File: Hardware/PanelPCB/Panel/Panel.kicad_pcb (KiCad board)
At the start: 2 copper layers, 22 x 32 mm, 13 parts, among them J1 RJ45, J2 Conn_01x03_Socket, U1 AP2204R-5.0, U2 SN74LV1T34DBV

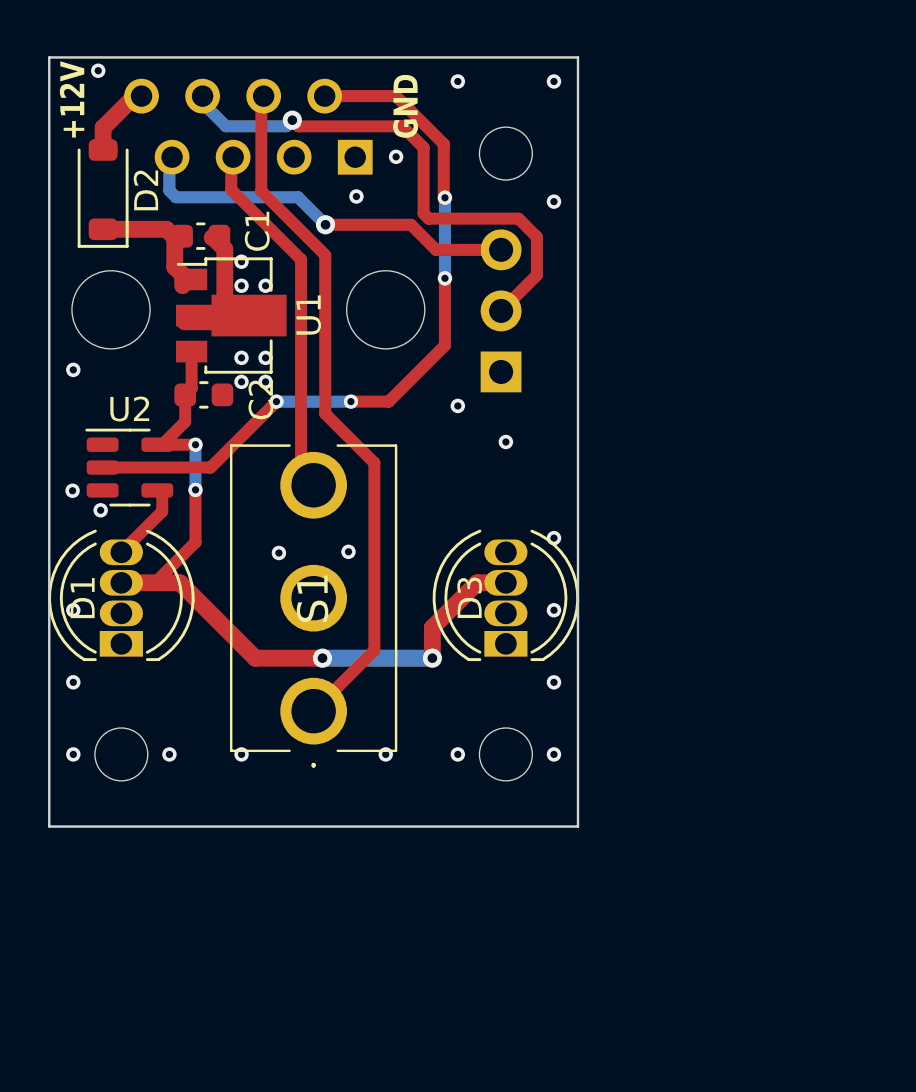
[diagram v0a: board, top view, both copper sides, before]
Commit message: update ControlPanel PCB
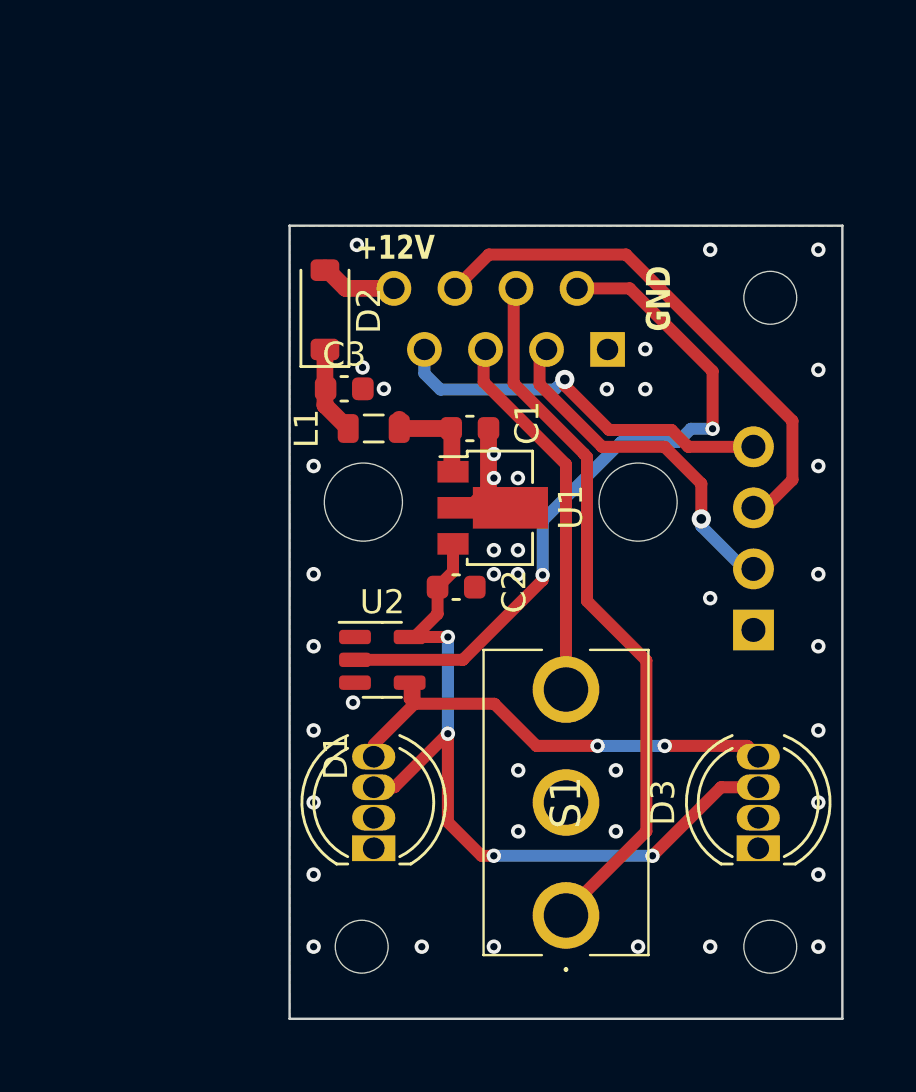
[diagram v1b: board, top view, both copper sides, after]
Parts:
- added C3: 100nF, Capacitor_SMD:C_0603_1608Metric, F.Cu at (152.3, 73.8)
- added L1: L_Ferrite, Inductor_SMD:L_0805_2012Metric, F.Cu at (153.5, 75.4)
- J2: footprint Connector_PinHeader_2.54mm:PinHeader_1x03_P2.54mm_Vertical -> Connector_PinHeader_2.54mm:PinHeader_1x04_P2.54mm_Vertical
- moved J2 15.0 mm to (169.3, 83.8)
- moved C1 13.8 mm to (157.5, 75.4)
- moved H3 13.6 mm to (170.0, 97.0)
- moved U1 13.5 mm to (158.8, 78.7)
- moved C2 13.2 mm to (156.9, 82.0)
- moved J1 13.2 mm to (163.2, 72.2)
- moved U2 13.2 mm to (153.9, 85.1)
- moved H2 12.8 mm to (153.0, 97.0)
- moved H1 12.5 mm to (170.0, 70.0)
- moved D1 12.4 mm to (153.5, 91.0)
- moved D3 12.4 mm to (169.5, 91.0)
- moved S1 11.2 mm to (161.5, 91.0)
- moved D2 10.5 mm to (151.5, 70.5)
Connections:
- C1 pad 1: Net-(D2-K) -> Net-(U1-VIN)
- J1 pad 3: unconnected-(J1-Pad3) -> OUT2
- J2 pad 2: IN3 -> OUT2
- J2 pad 3: IN4 -> IN3
- U1 pad 1: Net-(D2-K) -> Net-(U1-VIN)
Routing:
- net OUT_1: track 3.28 -> 19.5 mm, vias 0 -> 2
- net OUT2: track 0.00 -> 14.7 mm, vias 0 -> 1
- net Net-(U1-VIN): track 0.00 -> 4.37 mm
- net Net-(D2-K): track 5.00 -> 3.69 mm
- net IN1: track 28.7 -> 29.5 mm
- net OUT1: track 30.6 -> 29.8 mm, vias 4 -> 2
- net GND1: track 5.13 -> 4.28 mm, vias 31 -> 41
- net +5V: track 33.2 -> 32.5 mm
- net IN3: track 22.1 -> 22.0 mm, vias 1 -> 0
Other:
- board size 22 x 32 mm -> 23 x 33 mm

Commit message: update PanelPCB and generade a DualPanelPCB
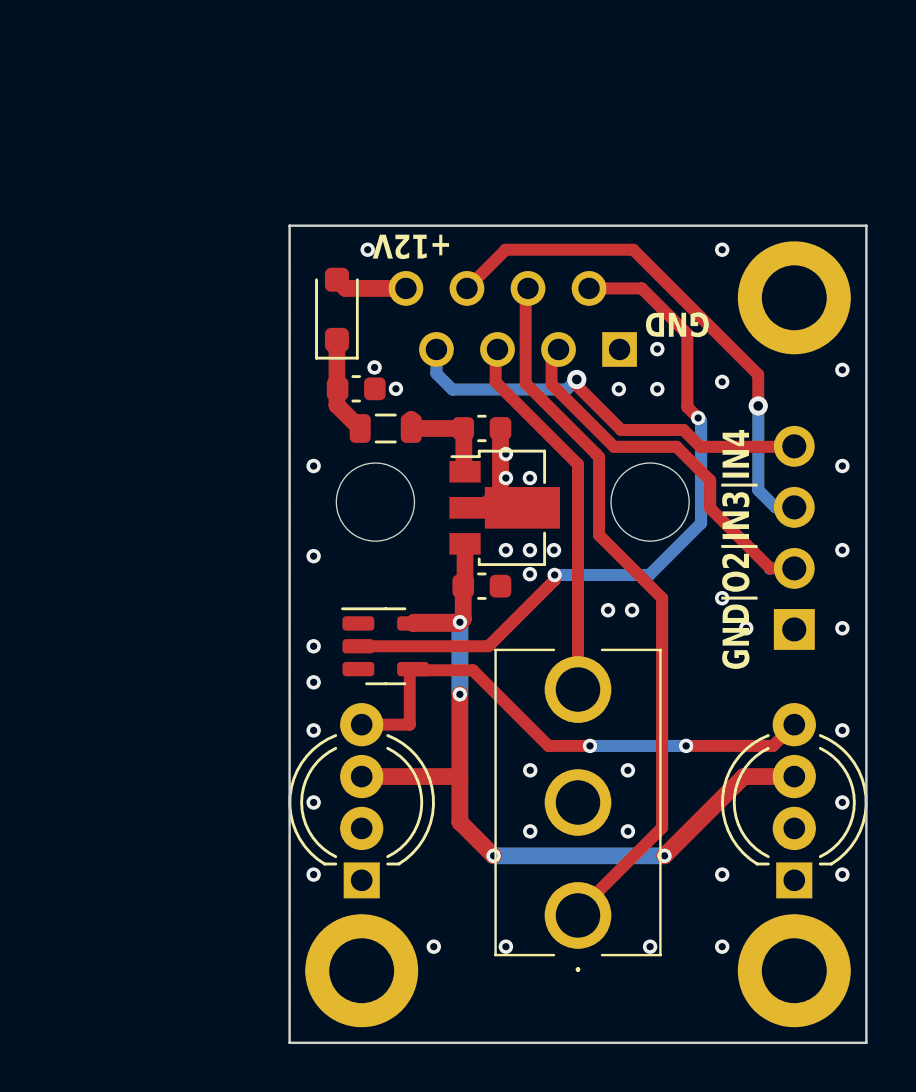
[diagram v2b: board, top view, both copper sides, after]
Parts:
- D1, D3: footprint LED_THT:LED_D5.0mm-4_RGB -> LED_THT:LED_D5.0mm-4_RGB_Wide_Pins
- D2: value 1N4148W -> CUS15S30,H3F; footprint Diode_SMD:D_SOD-123 -> Diode_SMD:D_SOD-323_HandSoldering
- H1, H2, H3: footprint MountingHole:MountingHole_2.2mm_M2_DIN965 -> MountingHole:MountingHole_2.7mm_M2.5_DIN965_Pad
- moved J2 1.70 mm to (171.0, 83.8)
- moved D3 1.50 mm to (171.0, 91.0)
- moved H3 1.41 mm to (171.0, 98.0)
- moved C2 1.07 mm to (158.0, 82.0)
- moved H1 1.00 mm to (171.0, 70.0)
- moved H2 1.00 mm to (153.0, 98.0)
- moved U2 0.58 mm to (154.0, 84.5)
- moved C1 0.50 mm to (158.0, 75.4)
- moved C3 0.50 mm to (152.8, 73.8)
- moved D1 0.50 mm to (153.0, 91.0)
- moved D2 0.50 mm to (152.0, 70.5)
- moved J1 0.50 mm to (163.7, 72.2)
- moved L1 0.50 mm to (154.0, 75.4)
- moved S1 0.50 mm to (162.0, 91.0)
- moved U1 0.50 mm to (159.2, 78.7)
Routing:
- net +5V: track 32.5 -> 35.8 mm
- net OUT_1: track 19.5 -> 21.9 mm
- net IN4: track 16.7 -> 17.9 mm
- net OUT2: track 14.7 -> 15.6 mm, vias 1 -> 0
- net IN3: track 22.0 -> 21.5 mm, vias 0 -> 1
- net GND1: vias 41 -> 42
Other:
- board size 23 x 33 mm -> 24 x 34 mm
- board text added: "GND|O2|IN3|IN4"
- board text added: "IN4|IN3|O2|GND"
- board text removed: "IN4|IN3|GND"
